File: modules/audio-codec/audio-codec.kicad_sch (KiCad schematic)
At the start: 25 parts, among them U1 TLV320AIC3110IRHBR, U2 ADP5301ACBZ-1-R7

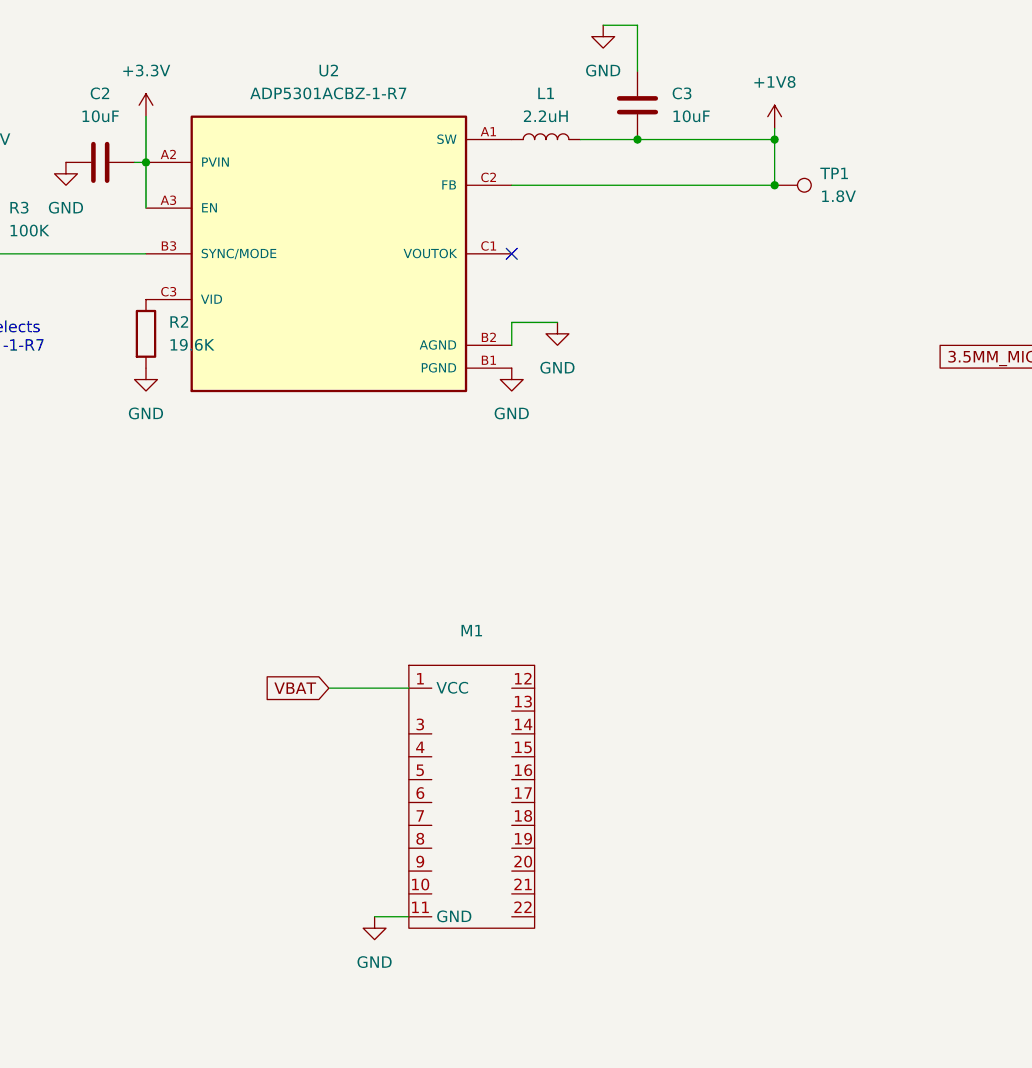
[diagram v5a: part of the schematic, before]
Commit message: more work on audio codec PCB layout
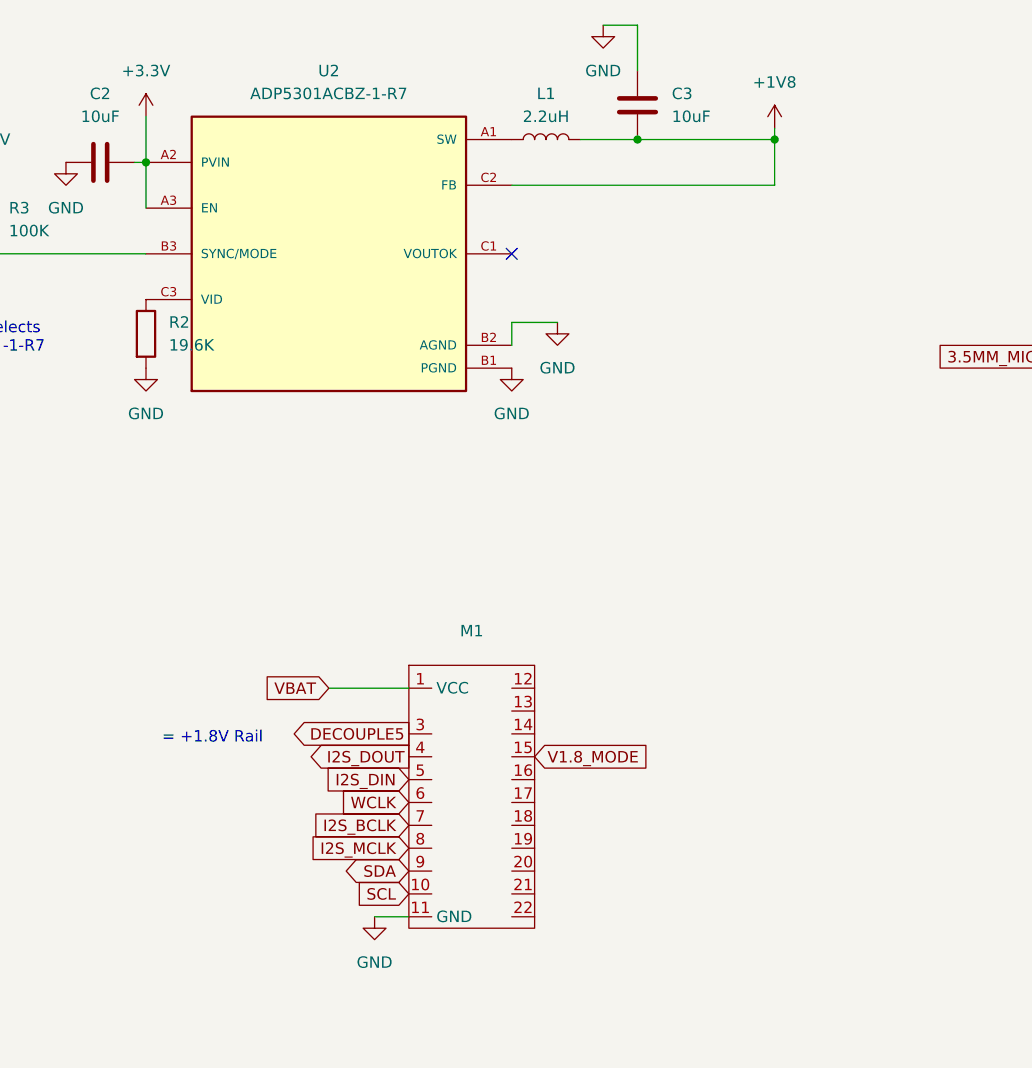
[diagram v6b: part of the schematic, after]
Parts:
- removed TP1: 1.8V, TestPoint:TestPoint_Pad_D1.0mm, symbol Connector:TestPoint
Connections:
- net +1V8: now also M1.3
- net I2S_BCLK: now also M1.7
- net I2S_DIN: now also M1.5
- net I2S_DOUT: now also M1.4
- net I2S_MCLK: now also M1.8
- net SCL: now also M1.10
- net SDA: now also M1.9
- net V1.8_MODE: now also M1.15
- net WCLK: now also M1.6
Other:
- note added: "= +1.8V Rail"
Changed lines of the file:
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@@
 	)
 	(junction
-		(at 134.62 57.15)
-		(diameter 0)
-		(color 0 0 0 0)
-	)
-	(junction
 		(at 119.38 52.07)
 		(diameter 0)
@@
 		)
 	)
+	(text "= +1.8V Rail"
+		(exclude_from_sim no)
+		(at 66.548 118.618 0)
+		(effects
+			(font
+				(size 1.27 1.27)
+			)
+			(justify left)
+		)
+	)
 	(text "DVSS & IOVSS tied to\ndigital side of GND\nplane.\n\nAll others to analog\n(VBAT) side."
 		(exclude_from_sim no)
@@
 		)
 	)
+	(global_label "WCLK"
+		(shape input)
+		(at 93.98 125.73 180)
+		(fields_autoplaced yes)
+		(effects
+			(font
+				(size 1.27 1.27)
+			)
+			(justify right)
+		)
+		(property "Intersheetrefs" "${INTERSHEET_REFS}"
+			(at 85.9753 125.73 0)
+			(effects
+				(font
+					(size 1.27 1.27)
+				)
+				(justify right)
+				(hide yes)
+			)
+		)
+	)
 	(global_label "DECOUPLE6"
 		(shape input)
@@
 		)
 	)
+	(global_label "I2S_MCLK"
+		(shape input)
+		(at 93.98 130.81 180)
+		(fields_autoplaced yes)
+		(effects
+			(font
+				(size 1.27 1.27)
+			)
+			(justify right)
+		)
+		(property "Intersheetrefs" "${INTERSHEET_REFS}"
+			(at 81.9839 130.81 0)
+			(effects
+				(font
+					(size 1.27 1.27)
+				)
+				(justify right)
+				(hide yes)
+			)
+		)
+	)
 	(global_label "I2S_DIN"
 		(shape input)
@@
 		)
 	)
+	(global_label "SCL"
+		(shape input)
+		(at 93.98 135.89 180)
+		(fields_autoplaced yes)
+		(effects
+			(font
+				(size 1.27 1.27)
+			)
+			(justify right)
+		)
+		(property "Intersheetrefs" "${INTERSHEET_REFS}"
+			(at 87.4872 135.89 0)
+			(effects
+				(font
+					(size 1.27 1.27)
+				)
+				(justify right)
+				(hide yes)
+			)
+		)
+	)
 	(global_label "3.5MM_MIC"
 		(shape input)
@@
 		)
 	)
+	(global_label "I2S_DOUT"
+		(shape output)
+		(at 93.98 120.65 180)
+		(fields_autoplaced yes)
+		(effects
+			(font
+				(size 1.27 1.27)
+			)
+			(justify right)
+		)
+		(property "Intersheetrefs" "${INTERSHEET_REFS}"
+			(at 82.1048 120.65 0)
+			(effects
+				(font
+					(size 1.27 1.27)
+				)
+				(justify right)
+				(hide yes)
+			)
+		)
+	)
 	(global_label "V1.8_MODE"
 		(shape input)
@@
 		)
 	)
+	(global_label "SDA"
+		(shape bidirectional)
+		(at 93.98 133.35 180)
+		(fields_autoplaced yes)
+		(effects
+			(font
+				(size 1.27 1.27)
+			)
+			(justify right)
+		)
+		(property "Intersheetrefs" "${INTERSHEET_REFS}"
+			(at 86.3154 133.35 0)
+			(effects
+				(font
+					(size 1.27 1.27)
+				)
+				(justify right)
+				(hide yes)
+			)
+		)
+	)
 	(global_label "DECOUPLE2"
 		(shape input)
@@
 		)
 	)
+	(global_label "V1.8_MODE"
+		(shape input)
+		(at 107.95 120.65 0)
+		(fields_autoplaced yes)
+		(effects
+			(font
+				(size 1.27 1.27)
+			)
+			(justify left)
+		)
+		(property "Intersheetrefs" "${INTERSHEET_REFS}"
+			(at 121.2161 120.65 0)
+			(effects
+				(font
+					(size 1.27 1.27)
+				)
+				(justify left)
+				(hide yes)
+			)
+		)
+	)
 	(global_label "DECOUPLE6"
 		(shape input)
@@
 		)
 	)
+	(global_label "I2S_BCLK"
+		(shape input)
+		(at 93.98 128.27 180)
+		(fields_autoplaced yes)
+		(effects
+			(font
+				(size 1.27 1.27)
+			)
+			(justify right)
+		)
+		(property "Intersheetrefs" "${INTERSHEET_REFS}"
+			(at 82.1653 128.27 0)
+			(effects
+				(font
+					(size 1.27 1.27)
+				)
+				(justify right)
+				(hide yes)
+			)
+		)
+	)
+	(global_label "I2S_DIN"
+		(shape input)
+		(at 93.98 123.19 180)
+		(fields_autoplaced yes)
+		(effects
+			(font
+				(size 1.27 1.27)
+			)
+			(justify right)
+		)
+		(property "Intersheetrefs" "${INTERSHEET_REFS}"
+			(at 83.7981 123.19 0)
+			(effects
+				(font
+					(size 1.27 1.27)
+				)
+				(justify right)
+				(hide yes)
+			)
+		)
+	)
 	(global_label "DECOUPLE1"
 		(shape input)
@@
 		)
 	)
+	(global_label "DECOUPLE5"
+		(shape output)
+		(at 93.98 118.11 180)
+		(fields_autoplaced yes)
+		(effects
+			(font
+				(size 1.27 1.27)
+			)
+			(justify right)
+		)
+		(property "Intersheetrefs" "${INTERSHEET_REFS}"
+			(at 79.9882 118.11 0)
+			(effects
+				(font
+					(size 1.27 1.27)
+				)
+				(justify right)
+				(hide yes)
+			)
+		)
+	)
 	(global_label "SPEAKER_L_M"
 		(shape output)
@@
 					(unit 1)
 				)
-			)
-		)
-	)
-	(symbol
-		(lib_id "Connector:TestPoint")
-		(at 134.62 57.15 270)
-		(unit 1)
-		(exclude_from_sim no)
-		(in_bom yes)
-		(on_board yes)
-		(dnp no)
-		(fields_autoplaced yes)
-		(property "Reference" "TP1"
-			(at 139.7 55.8799 90)
-			(effects
-				(font
-					(size 1.27 1.27)
-				)
-				(justify left)
-			)
-		)
-		(property "Value" "1.8V"
-			(at 139.7 58.4199 90)
-			(effects
-				(font
-					(size 1.27 1.27)
-				)
-				(justify left)
-			)
-		)
-		(property "Footprint" "TestPoint:TestPoint_Pad_D1.0mm"
-			(at 134.62 62.23 0)
-			(effects
-				(font
-					(size 1.27 1.27)
-				)
-				(hide yes)
-			)
-		)
-		(property "Datasheet" "~"
-			(at 134.62 62.23 0)
-			(effects
-				(font
-					(size 1.27 1.27)
-				)
-				(hide yes)
-			)
-		)
-		(property "Description" "test point"
-			(at 134.62 57.15 0)
-			(effects
-				(font
-					(size 1.27 1.27)
-				)
-				(hide yes)
-			)
-		)
-		(pin "1"
-		)
-		(instances
-			(project ""
-				(path "/e0031877-65b0-4e57-86fe-bc20869de862"
-					(reference "TP1")
-					(unit 1)
-				)

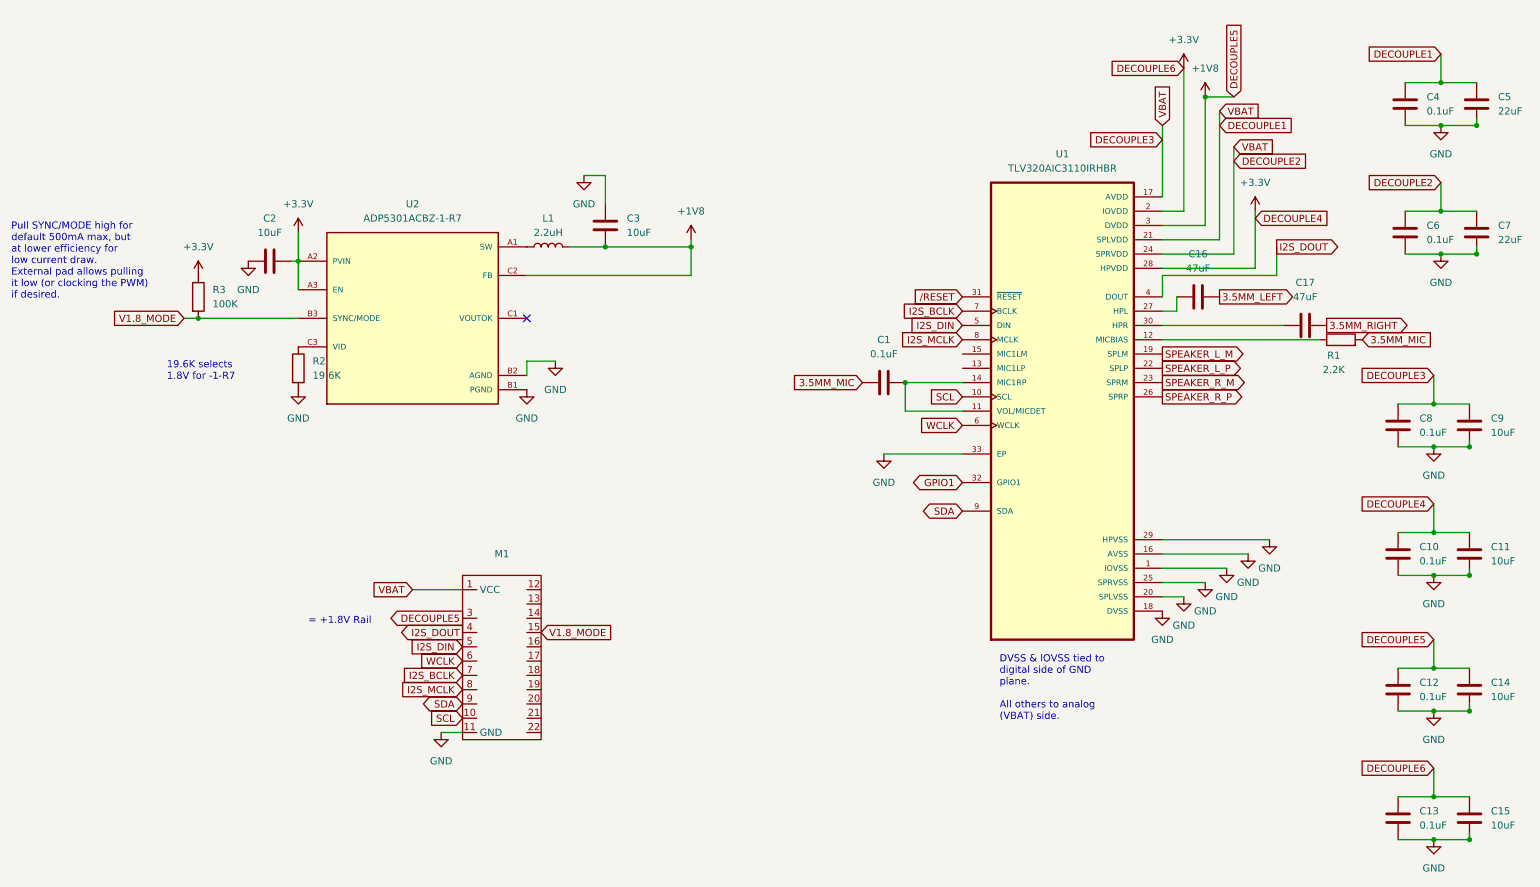
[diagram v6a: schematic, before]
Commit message: finish placing and routing audio codec module
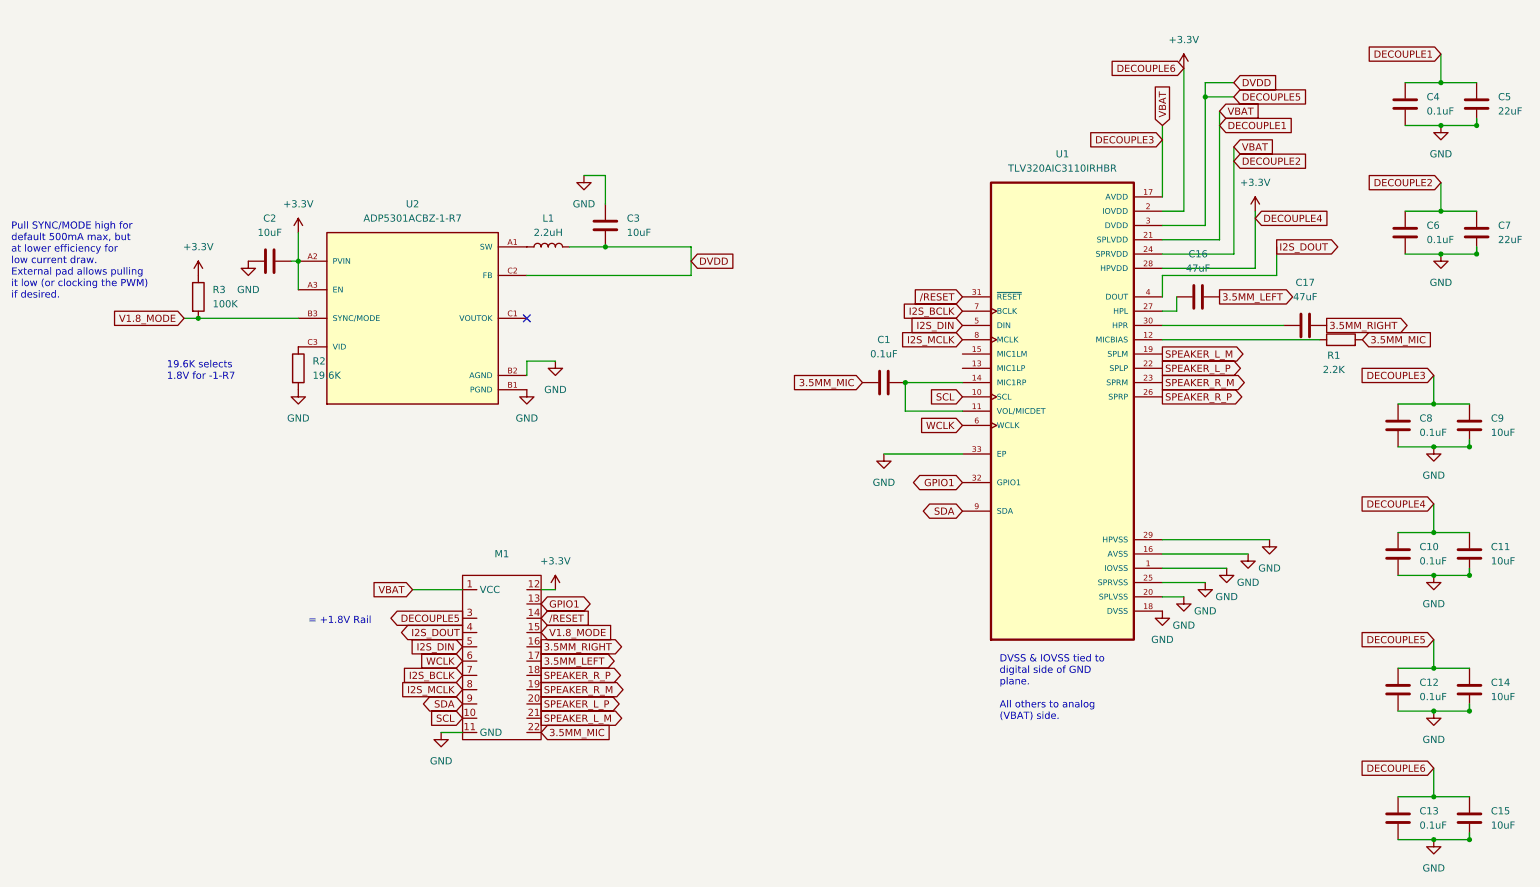
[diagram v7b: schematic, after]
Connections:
- net +3.3V: now also M1.12
- net 3.5MM_LEFT: now also M1.17
- net 3.5MM_MIC: now also M1.22
- net 3.5MM_RIGHT: now also M1.16
- net GPIO1: now also M1.13
- net SPEAKER_L_M: now also M1.21
- net SPEAKER_L_P: now also M1.20
- net SPEAKER_R_M: now also M1.19
- net SPEAKER_R_P: now also M1.18
- net /RESET: now also M1.14
- net +1V8 renamed DECOUPLE5

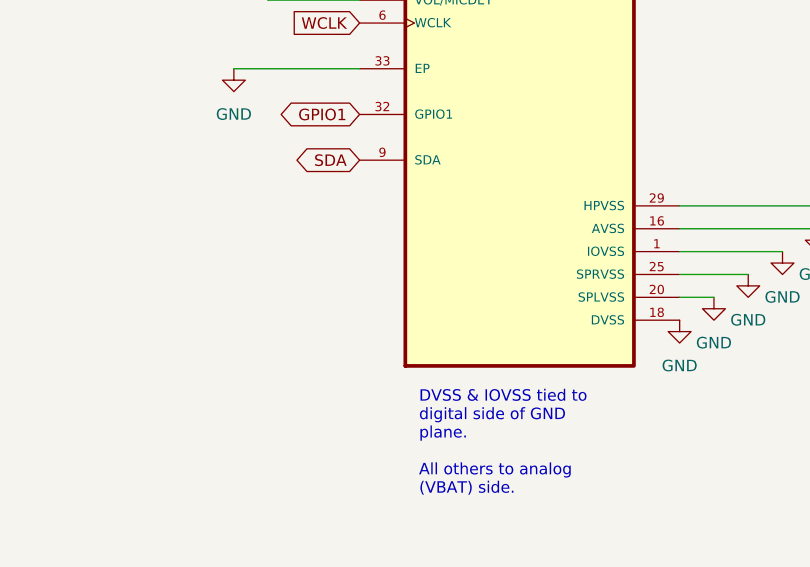
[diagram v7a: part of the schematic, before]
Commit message: add gnd pads to codec thermal pad, tidy passives and label on rear
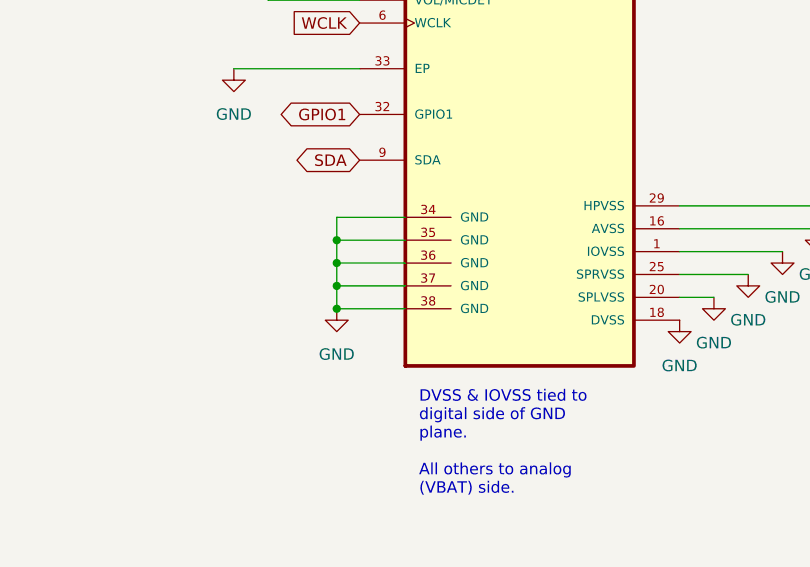
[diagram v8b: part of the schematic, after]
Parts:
- U1: footprint audio-codec:IC_ADS125H01IRHBT -> TLV320AIC3110IRHBR:IC_ADS125H01IRHBT
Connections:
- net GND: now also U1.34 (GND), U1.35 (GND), U1.36 (GND), U1.37 (GND), U1.38 (GND)
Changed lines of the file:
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@@
 	)
 	(junction
+		(at 180.34 107.95)
+		(diameter 0)
+		(color 0 0 0 0)
+	)
+	(junction
 		(at 266.7 134.62)
 		(diameter 0)
@@
 	)
 	(junction
+		(at 180.34 113.03)
+		(diameter 0)
+		(color 0 0 0 0)
+	)
+	(junction
 		(at 226.06 25.4)
 		(diameter 0)
@@
 	)
 	(junction
+		(at 180.34 110.49)
+		(diameter 0)
+		(color 0 0 0 0)
+	)
+	(junction
 		(at 266.7 149.86)
 		(diameter 0)
@@
 	)
 	(junction
+		(at 180.34 115.57)
+		(diameter 0)
+		(color 0 0 0 0)
+	)
+	(junction
 		(at 46.99 64.77)
 		(diameter 0)
@@
 	(wire
 		(pts
+			(xy 180.34 110.49) (xy 187.96 110.49)
+		)
+		(stroke
+			(width 0)
+			(type default)
+		)
+	)
+	(wire
+		(pts
 			(xy 273.05 109.22) (xy 273.05 110.49)
 		)
@@
 	(wire
 		(pts
+			(xy 180.34 113.03) (xy 180.34 115.57)
+		)
+		(stroke
+			(width 0)
+			(type default)
+		)
+	)
+	(wire
+		(pts
 			(xy 260.35 87.63) (xy 266.7 87.63)
 		)
@@
 	(wire
 		(pts
+			(xy 180.34 115.57) (xy 187.96 115.57)
+		)
+		(stroke
+			(width 0)
+			(type default)
+		)
+	)
+	(wire
+		(pts
 			(xy 218.44 50.8) (xy 228.6 50.8)
 		)
@@
 	(wire
 		(pts
+			(xy 180.34 113.03) (xy 187.96 113.03)
+		)
+		(stroke
+			(width 0)
+			(type default)
+		)
+	)
+	(wire
+		(pts
 			(xy 274.32 52.07) (xy 274.32 53.34)
 		)
@@
 	(wire
 		(pts
+			(xy 187.96 105.41) (xy 180.34 105.41)
+		)
+		(stroke
+			(width 0)
+			(type default)
+		)
+	)
+	(wire
+		(pts
 			(xy 266.7 87.63) (xy 273.05 87.63)
 		)
@@
 	(wire
 		(pts
+			(xy 180.34 107.95) (xy 187.96 107.95)
+		)
+		(stroke
+			(width 0)
+			(type default)
+		)
+	)
+	(wire
+		(pts
+			(xy 180.34 107.95) (xy 180.34 110.49)
+		)
+		(stroke
+			(width 0)
+			(type default)
+		)
+	)
+	(wire
+		(pts
 			(xy 85.09 113.03) (xy 93.98 113.03)
 		)
@@
 	(wire
 		(pts
+			(xy 180.34 105.41) (xy 180.34 107.95)
+		)
+		(stroke
+			(width 0)
+			(type default)
+		)
+	)
+	(wire
+		(pts
 			(xy 218.44 66.04) (xy 240.03 66.04)
 		)
@@
 	(wire
 		(pts
+			(xy 180.34 110.49) (xy 180.34 113.03)
+		)
+		(stroke
+			(width 0)
+			(type default)
+		)
+	)
+	(wire
+		(pts
 			(xy 220.98 60.96) (xy 220.98 63.5)
 		)
@@
 			)
 		)
-		(property "Footprint" "audio-codec:IC_ADS125H01IRHBT"
+		(property "Footprint" "TLV320AIC3110IRHBR:IC_ADS125H01IRHBT"
 			(at 200.66 81.28 0)
 			(effects
@@
 		(pin "15"
 		)
+		(pin "37"
+		)
+		(pin "35"
+		)
+		(pin "38"
+		)
+		(pin "34"
+		)
+		(pin "36"
+		)
 		(instances
 			(project ""
@@
 					(unit 1)
 				)
+			)
+		)
+	)
+	(symbol
+		(lib_id "power:GND")
+		(at 180.34 115.57 0)
+		(unit 1)
+		(exclude_from_sim no)
+		(in_bom yes)
+		(on_board yes)
+		(dnp no)
+		(fields_autoplaced yes)
+		(property "Reference" "#PWR04"
+			(at 180.34 121.92 0)
+			(effects
+				(font
+					(size 1.27 1.27)
+				)
+				(hide yes)
+			)
+		)
+		(property "Value" "GND"
+			(at 180.34 120.65 0)
+			(effects
+				(font
+					(size 1.27 1.27)
+				)
+			)
+		)
+		(property "Footprint" ""
+			(at 180.34 115.57 0)
+			(effects
+				(font
+					(size 1.27 1.27)
+				)
+				(hide yes)
+			)
+		)
+		(property "Datasheet" ""
+			(at 180.34 115.57 0)
+			(effects
+				(font
+					(size 1.27 1.27)
+				)
+				(hide yes)
+			)
+		)
+		(property "Description" "Power symbol creates a global label with name \"GND\" , ground"
+			(at 180.34 115.57 0)
+			(effects
+				(font
+					(size 1.27 1.27)
+				)
+				(hide yes)
+			)
+		)
+		(pin "1"
+		)
+		(instances
+			(project "audio-codec"
+				(path "/e0031877-65b0-4e57-86fe-bc20869de862"
+					(reference "#PWR04")
+					(unit 1)
+				)
